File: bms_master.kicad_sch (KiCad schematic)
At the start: 61 parts, among them J1 I2C1, J2 SWD, J3 I2C2, J4 Conn_01x05, J5 Conn_01x05, J6 Conn_01x08, SW1 SW_Push, U1 SN65HVD1050D, U2 STM32F103C8Tx, U3 MAX6126, U4 MAX11163, U5 M24C64-R, U6 741G3157, U7 TPS7B88, U8 MCP1700x-330xxMB, Y1 8M

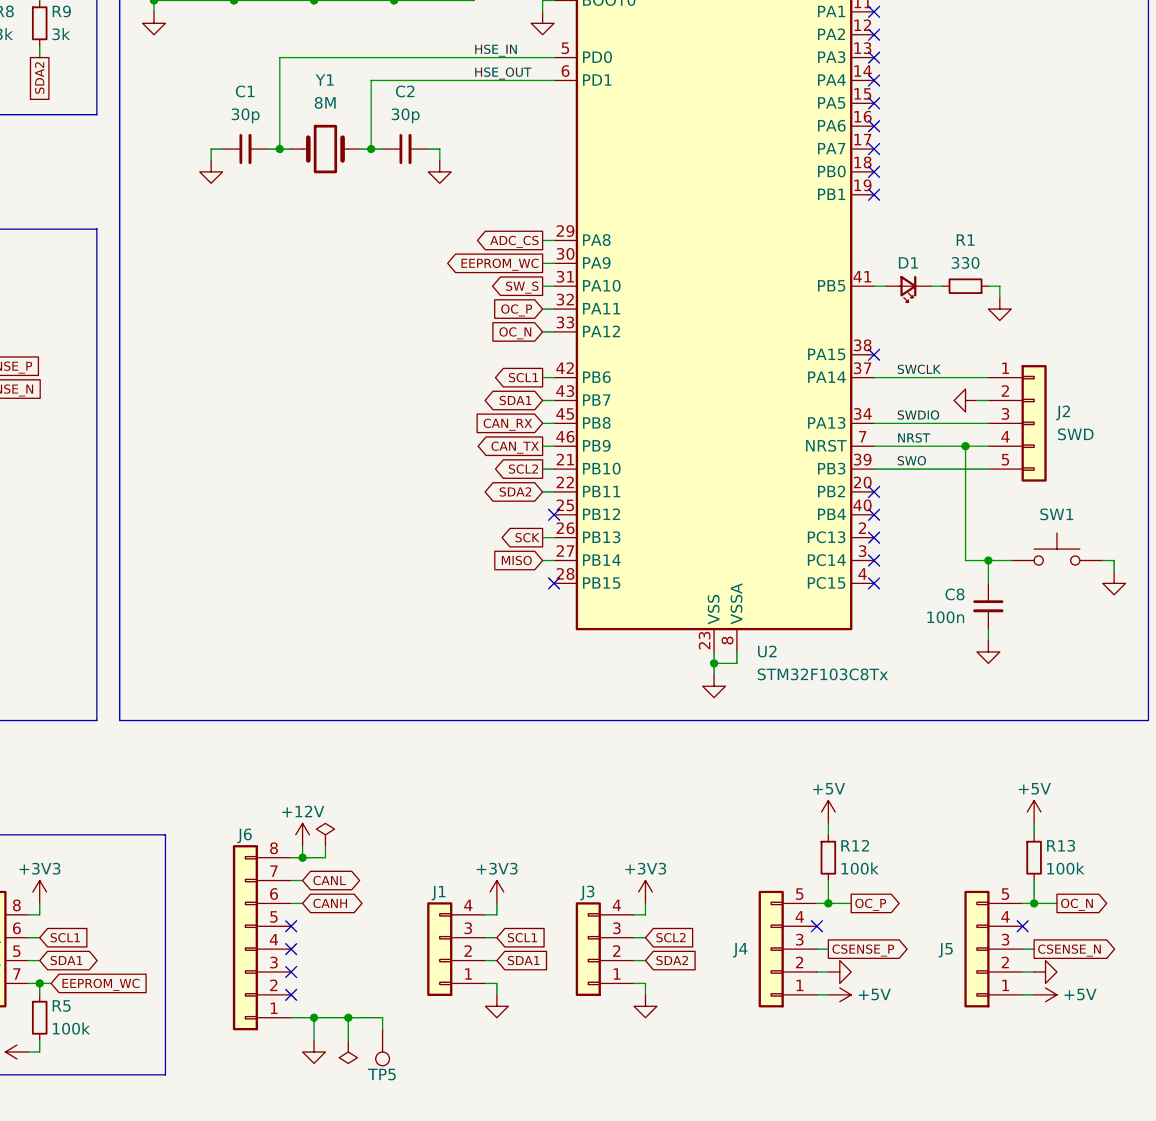
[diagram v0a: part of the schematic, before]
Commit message: schematic: Add shutdown and charge enable outputs
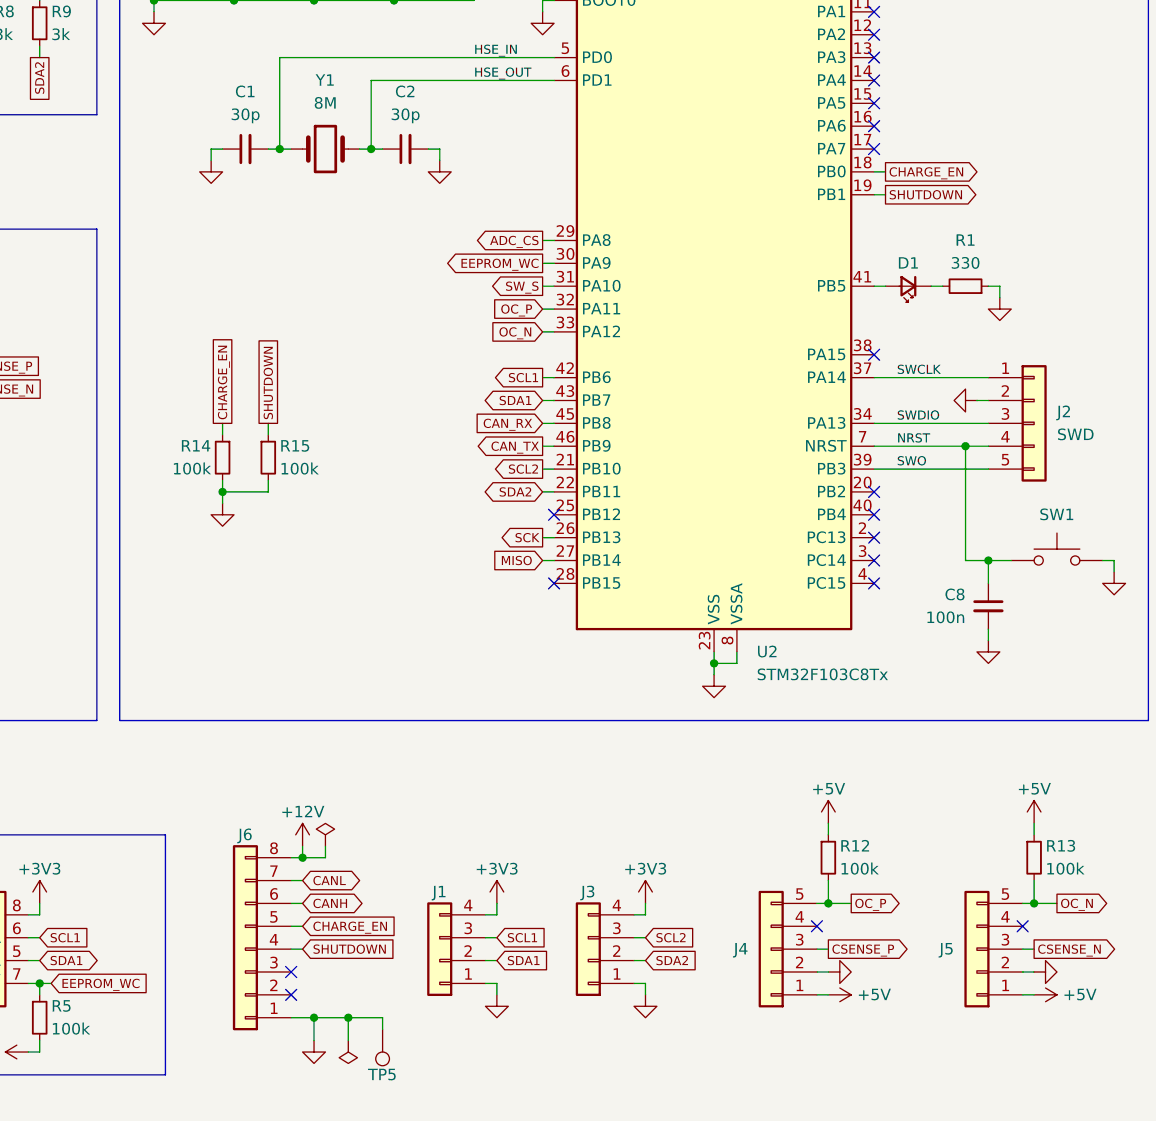
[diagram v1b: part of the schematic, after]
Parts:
- added R14, R15: 100k, symbol Device:R_Small
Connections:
- net GND: now also R14.2, R15.2
- net SHUTDOWN: now reaches J6.4 (Pin_4)
- net SHUTDOWN: now also U2.19 (PB1), R15.1
- net CHARGE_EN: now reaches J6.5 (Pin_5)
- net CHARGE_EN: now also U2.18 (PB0), R14.1
- no-connect marks 25 -> 21

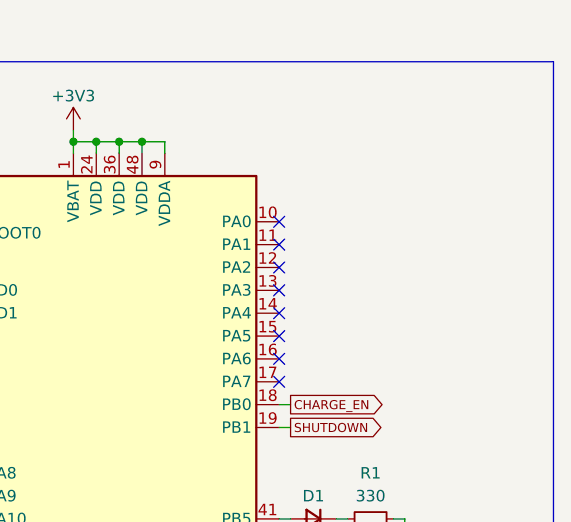
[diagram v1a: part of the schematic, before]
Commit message: schematic: Measure 12V rail with STM ADC
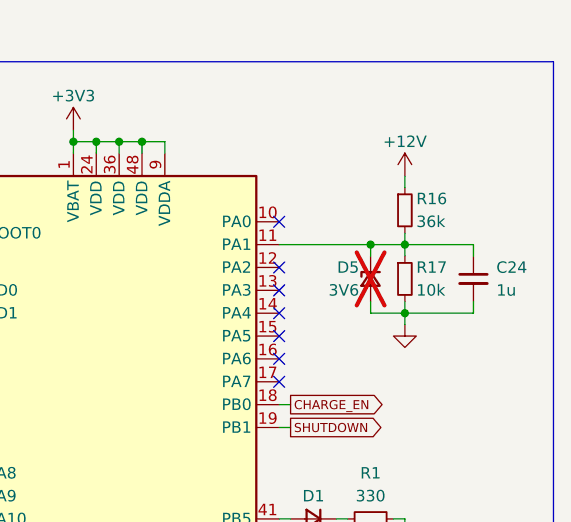
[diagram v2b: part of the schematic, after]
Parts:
- added C24: 1u, symbol Device:C_Small
- added D5: 3V6, symbol Device:D_Zener_Small
- added R16: 36k, symbol Device:R_Small
- added R17: 10k, symbol Device:R_Small
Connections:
- net +12V: now also R16.1
- net GND: now also C24.2, D5.2 (A), R17.2
- net at U2.11 (PA1): now also C24.1, D5.1 (K), R16.2, R17.1
- no-connect marks 21 -> 20

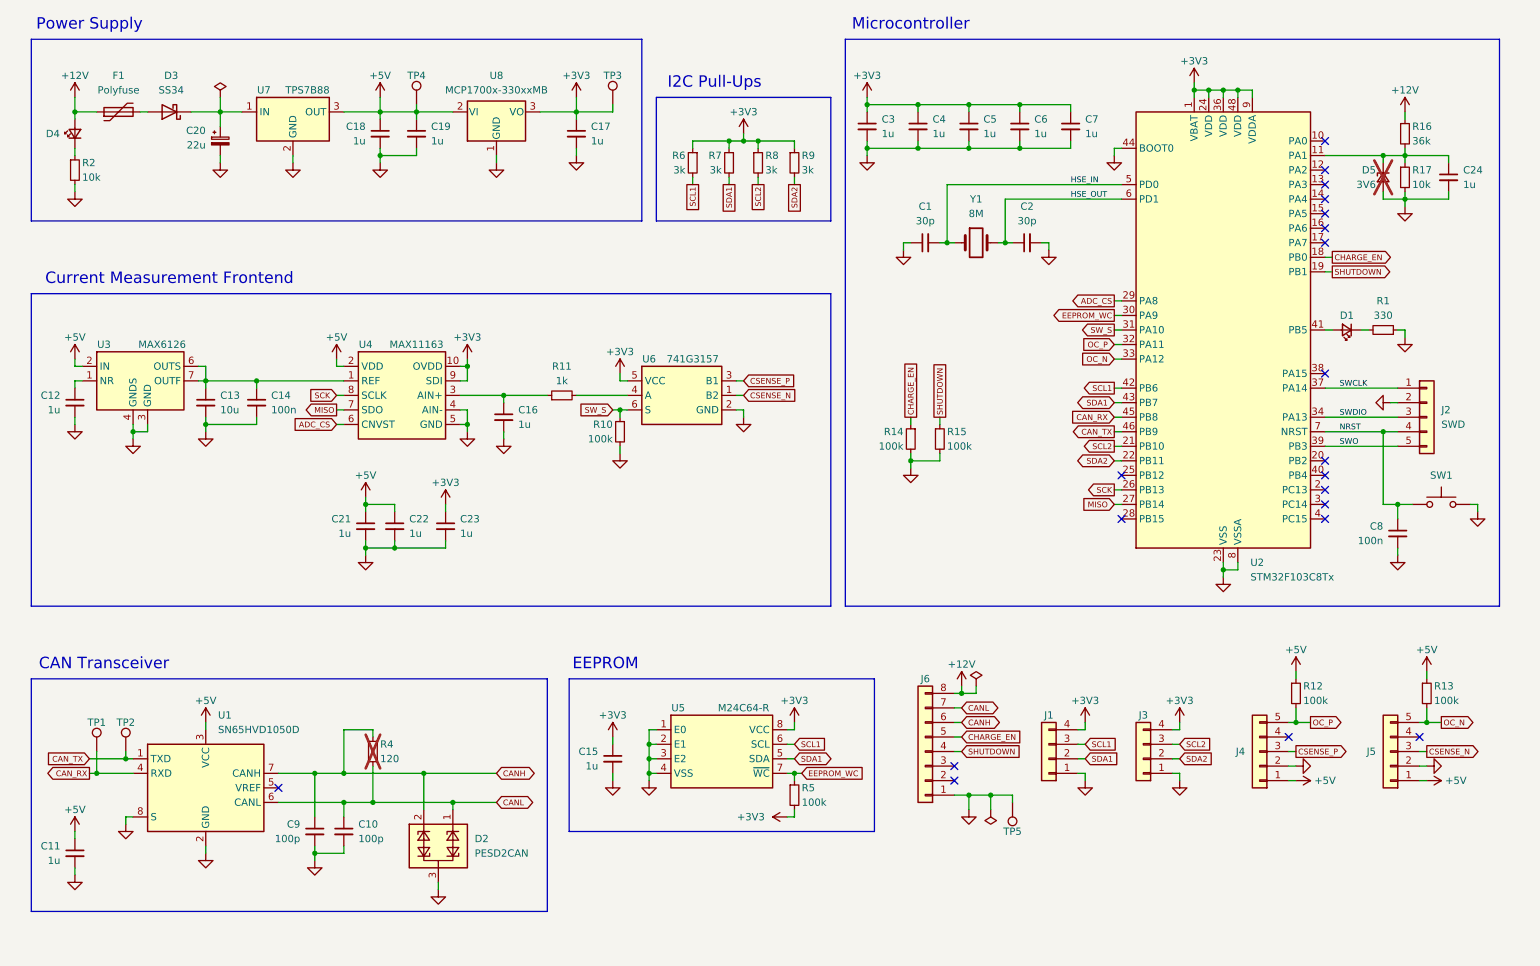
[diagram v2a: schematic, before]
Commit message: schematic: Re-annotate designators
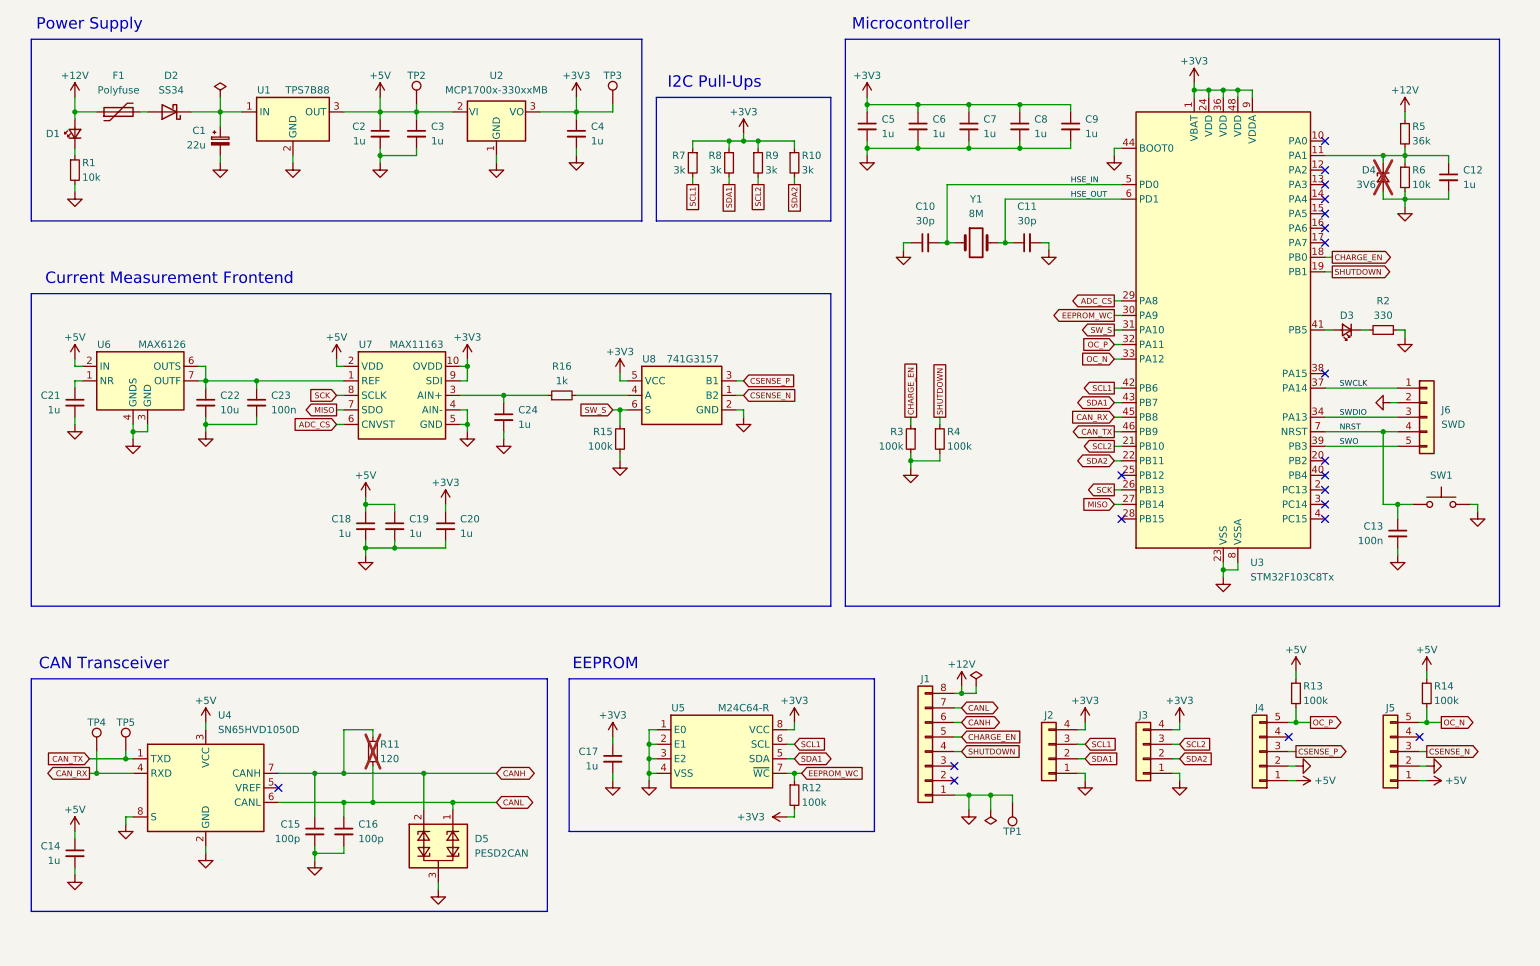
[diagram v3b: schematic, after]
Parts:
- renumbered C20 to C1, C1 to C10, C2 to C11, C24 to C12, C8 to C13, C11 to C14, C9 to C15, C10 to C16, C15 to C17, C21 to C18, C22 to C19, C18 to C2, C23 to C20, C12 to C21, C13 to C22, C14 to C23, C16 to C24, C19 to C3, C17 to C4, C3 to C5, C4 to C6, C5 to C7, C6 to C8, C7 to C9, D4 to D1, D3 to D2, D1 to D3, D5 to D4, D2 to D5, J6 to J1, J1 to J2, J2 to J6, R2 to R1, R9 to R10, R4 to R11, R5 to R12, R12 to R13, R13 to R14, R10 to R15, R11 to R16, R1 to R2, R14 to R3, R15 to R4, R16 to R5, R17 to R6, R6 to R7, R7 to R8, R8 to R9, TP5 to TP1, TP4 to TP2, TP1 to TP4, TP2 to TP5, U7 to U1, U8 to U2, U2 to U3, U1 to U4, U3 to U6, U4 to U7, U6 to U8
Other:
- moved on the sheet: R15

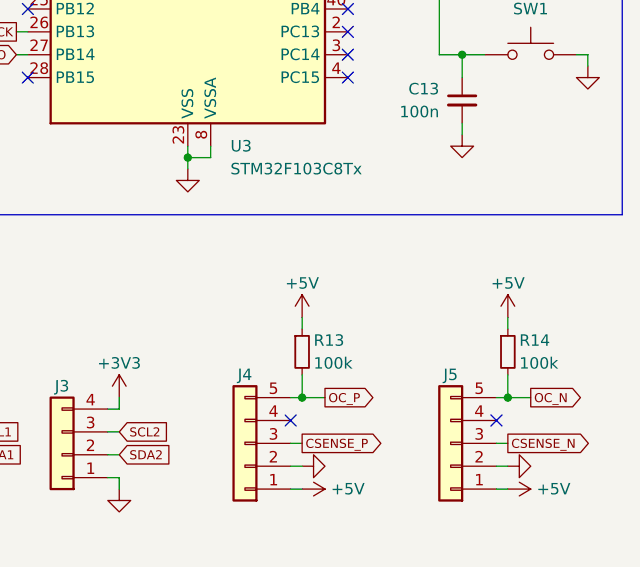
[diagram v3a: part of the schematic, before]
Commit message: schematic: Fix overcurrent pin pull-up voltage
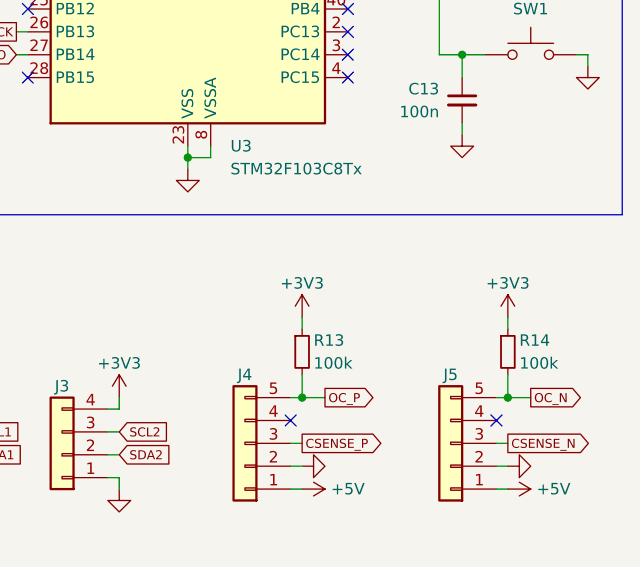
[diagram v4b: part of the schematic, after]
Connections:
- net +3V3: now also R13.1, R14.1
- net +5V: no longer R13.1, R14.1
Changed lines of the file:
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@@
 	)
 	(symbol
+		(lib_id "power:+3V3")
+		(at 264.16 132.08 0)
+		(unit 1)
+		(exclude_from_sim no)
+		(in_bom yes)
+		(on_board yes)
+		(dnp no)
+		(property "Reference" "#PWR090"
+			(at 264.16 135.89 0)
+			(effects
+				(font
+					(size 1.27 1.27)
+				)
+				(hide yes)
+			)
+		)
+		(property "Value" "+3V3"
+			(at 264.16 128.27 0)
+			(effects
+				(font
+					(size 1.27 1.27)
+				)
+			)
+		)
+		(property "Footprint" ""
+			(at 264.16 132.08 0)
+			(effects
+				(font
+					(size 1.27 1.27)
+				)
+				(hide yes)
+			)
+		)
+		(property "Datasheet" ""
+			(at 264.16 132.08 0)
+			(effects
+				(font
+					(size 1.27 1.27)
+				)
+				(hide yes)
+			)
+		)
+		(property "Description" "Power symbol creates a global label with name \"+3V3\""
+			(at 264.16 132.08 0)
+			(effects
+				(font
+					(size 1.27 1.27)
+				)
+				(hide yes)
+			)
+		)
+		(pin "1"
+		)
+		(instances
+			(project "bms_master"
+				(path "/ff788b45-a486-492a-a3f3-4e15ca08a026"
+					(reference "#PWR090")
+					(unit 1)
+				)
+			)
+		)
+	)
+	(symbol
 		(lib_id "power:GND")
 		(at 27.94 48.26 0)
@@
 	)
 	(symbol
+		(lib_id "power:+3V3")
+		(at 241.3 132.08 0)
+		(unit 1)
+		(exclude_from_sim no)
+		(in_bom yes)
+		(on_board yes)
+		(dnp no)
+		(property "Reference" "#PWR089"
+			(at 241.3 135.89 0)
+			(effects
+				(font
+					(size 1.27 1.27)
+				)
+				(hide yes)
+			)
+		)
+		(property "Value" "+3V3"
+			(at 241.3 128.27 0)
+			(effects
+				(font
+					(size 1.27 1.27)
+				)
+			)
+		)
+		(property "Footprint" ""
+			(at 241.3 132.08 0)
+			(effects
+				(font
+					(size 1.27 1.27)
+				)
+				(hide yes)
+			)
+		)
+		(property "Datasheet" ""
+			(at 241.3 132.08 0)
+			(effects
+				(font
+					(size 1.27 1.27)
+				)
+				(hide yes)
+			)
+		)
+		(property "Description" "Power symbol creates a global label with name \"+3V3\""
+			(at 241.3 132.08 0)
+			(effects
+				(font
+					(size 1.27 1.27)
+				)
+				(hide yes)
+			)
+		)
+		(pin "1"
+		)
+		(instances
+			(project "bms_master"
+				(path "/ff788b45-a486-492a-a3f3-4e15ca08a026"
+					(reference "#PWR089")
+					(unit 1)
+				)
+			)
+		)
+	)
+	(symbol
 		(lib_id "bms_master:PESD2CAN")
 		(at 86.36 158.75 0)
@@
 	)
 	(symbol
-		(lib_id "power:+5V")
-		(at 264.16 132.08 0)
-		(unit 1)
-		(exclude_from_sim no)
-		(in_bom yes)
-		(on_board yes)
-		(dnp no)
-		(property "Reference" "#PWR09"
-			(at 264.16 135.89 0)
-			(effects
-				(font
-					(size 1.27 1.27)
-				)
-				(hide yes)
-			)
-		)
-		(property "Value" "+5V"
-			(at 264.16 128.27 0)
-			(effects
-				(font
-					(size 1.27 1.27)
-				)
-			)
-		)
-		(property "Footprint" ""
-			(at 264.16 132.08 0)
-			(effects
-				(font
-					(size 1.27 1.27)
-				)
-				(hide yes)
-			)
-		)
-		(property "Datasheet" ""
-			(at 264.16 132.08 0)
-			(effects
-				(font
-					(size 1.27 1.27)
-				)
-				(hide yes)
-			)
-		)
-		(property "Description" "Power symbol creates a global label with name \"+5V\""
-			(at 264.16 132.08 0)
-			(effects
-				(font
-					(size 1.27 1.27)
-				)
-				(hide yes)
-			)
-		)
-		(pin "1"
-		)
-		(instances
-			(project "bms_master"
-				(path "/ff788b45-a486-492a-a3f3-4e15ca08a026"
-					(reference "#PWR09")
-					(unit 1)
-				)
-			)
-		)
-	)
-	(symbol
 		(lib_id "power:GND")
 		(at 241.3 148.59 90)
@@
 					(unit 1)
 				)
-			)
-		)
-	)
-	(symbol
-		(lib_id "power:+5V")
-		(at 241.3 132.08 0)
-		(unit 1)
-		(exclude_from_sim no)
-		(in_bom yes)
-		(on_board yes)
-		(dnp no)
-		(property "Reference" "#PWR08"
-			(at 241.3 135.89 0)
-			(effects
-				(font
-					(size 1.27 1.27)
-				)
-				(hide yes)
-			)
-		)
-		(property "Value" "+5V"
-			(at 241.3 128.27 0)
-			(effects
-				(font
-					(size 1.27 1.27)
-				)
-			)
-		)
-		(property "Footprint" ""
-			(at 241.3 132.08 0)
-			(effects
-				(font
-					(size 1.27 1.27)
-				)
-				(hide yes)
-			)
-		)
-		(property "Datasheet" ""
-			(at 241.3 132.08 0)
-			(effects
-				(font
-					(size 1.27 1.27)
-				)
-				(hide yes)
-			)
-		)
-		(property "Description" "Power symbol creates a global label with name \"+5V\""
-			(at 241.3 132.08 0)
-			(effects
-				(font
-					(size 1.27 1.27)
-				)
-				(hide yes)
-			)
-		)
-		(pin "1"
-		)
-		(instances
-			(project "bms_master"
-				(path "/ff788b45-a486-492a-a3f3-4e15ca08a026"
-					(reference "#PWR08")
-					(unit 1)
-				)
